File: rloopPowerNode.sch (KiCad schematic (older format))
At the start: 82 parts

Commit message: BMS added ctrl pins, both fault outputs to MCU, ...
added a few more comments for component selection

directions on net labels
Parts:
- removed JP? (x6): Jumper_NC_Small, symbol Jumper_NC_Small
- removed P?: CONN_01X02, symbol CONN_01X02
- removed Q?: NMOS, symbol Q_NMOS_GDSD
- added D? (x2): ZENER +3V6, symbol ZENER
- added D?: LED, symbol Led_Small
- added D?: D, symbol D_Small
- added R?: 1K8, symbol R
- added R?: 330, symbol R
- added R? (x2): 470, symbol R
- added R?: 100K, symbol R
- added R? (x2): 10K, symbol R
- D? (x2): Watts (none) -> 500mW
- Q?: Imax (none) -> 1A (4 * 250mA); Vgs Thresh (none) -> < 3V
- Q?: Vgs Thresh (none) -> > -3V
- R?: Power (none) -> 2W
- R?: Power (none) -> 8W
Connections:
- net labels added: BMS-CS, BMS-MISO, BMS-MOSI, BMS-PWRAVAIL, BMS-PWRDN, BMS-PWREN, BMS-SCK, GNDFAULT-PWM
- net labels removed: BMS-PWR, OSBMS-CS, OSBMS-MISO, OSBMS-MOSI, OSBMS-SCK
- wire segments 380 -> 394
- no-connect marks 3 -> 4
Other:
- note added: "Precharge\nminimizes arcing in relays"
- note removed: "connect to ISOMETER HV"
- note removed: "ground fault event\nwill kill all relays"
- moved on the sheet: C?, D?, P?, R?, U?

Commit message: added footprint
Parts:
- C1, C10, C2, C3, C4, C8, C9: renamed from C?; footprint (none) -> Capacitors_SMD:C_0603
- C5, C7: renamed from C?; footprint (none) -> SMD_Packages:SMD-1210_Pol
- C6: renamed from C?; footprint (none) -> Capacitors_SMD:C_0805
- D1, D10, D11, D3, D4, D7, D9: renamed from D?; footprint (none) -> Diodes_SMD:SOD-123
- D2, D8: renamed from D?; footprint (none) -> LEDs:LED_0603
- D5, D6: renamed from D?; footprint (none) -> Diodes_SMD:SMC_Standard
- JP1, JP2: renamed from JP?; footprint (none) -> -footprints:SOLDERJUMPER
- P22: renamed from P?; footprint (none) -> -footprints:AMPMODU-02X05-0.05in; symbol CONN_02X05 -> AMPMODU-02X05
- Q1: renamed from Q?; footprint (none) -> TO_SOT_Packages_SMD:SOT-23
- Q2: renamed from Q?; footprint (none) -> -footprints:D-Pak_TO252AA
- R1, R15, R17, R18, R19, R2, R20, R21, R3, R4, R5, R6, R7: renamed from R?; footprint (none) -> Resistors_SMD:R_0603
- R11, R12, R13, R14, R16: renamed from R?; footprint (none) -> Resistors_SMD:R_1206_HandSoldering
- U1, U2, U5, U6: renamed from U?; footprint (none) -> -footprints:CPC1718
- U10: renamed from U?; footprint (none) -> -footprints:SOIC-8-W
- U3: renamed from U?; footprint MFSOP-6 -> -footprints:OPTOCOUPLER-0.1in-6pin-SMD
- U4: renamed from U?; footprint (none) -> TO_SOT_Packages_SMD:SOT-23-5
- U7: renamed from U?; footprint (none) -> Housings_SOIC:SOIC-8_3.9x4.9mm_Pitch1.27mm
- U8: renamed from U?; footprint (none) -> -footprints:MS56xx
- U9: renamed from U?; footprint (none) -> TO_SOT_Packages_SMD:SOT89-3_Housing
- gave numbers to parts that had none: 31
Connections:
- wire segments 394 -> 329

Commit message: more parts assigned
just a check in for the meeting
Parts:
- F1: footprint (none) -> Fuse_Holders_and_Fuses:BladeFuse-CarType
- F2: footprint (none) -> Resistors_ThroughHole:Resistor_Horizontal_RM15mm
- JP3: footprint (none) -> Pin_Headers:Pin_Header_Straight_1x03
- P1, P19, P2, P20, P21, P23, P3, P4: footprint (none) -> -footprints:CONN-JST-XH-2-PTH-RGT
- P15, P16, P5: footprint (none) -> -footprints:SCREWPAD-4-40
- P17: footprint (none) -> -footprints:CONN-JST-XH-8-PTH-RGT
- P18, P6, P7: footprint (none) -> -footprints:CONN-TE-MICROMNL-2-PTH-MALE-RGT
- R10, R9: footprint (none) -> -footprints:D-Pak-TO252AA-Resistor
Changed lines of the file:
@@
 F 0 "P1" H 13400 1600 50  0000 C CNN
 F 1 "CONN_01X02" V 13500 1450 50  0000 C CNN
-F 2 "" H 13400 1450 50  0001 C CNN
+F 2 "-footprints:CONN-JST-XH-2-PTH-RGT" H 13400 1450 50  0001 C CNN
 F 3 "" H 13400 1450 50  0000 C CNN
 	1    13400 1450
@@
 F 0 "P3" H 13400 2750 50  0000 C CNN
 F 1 "CONN_01X02" V 13500 2600 50  0000 C CNN
-F 2 "" H 13400 2600 50  0001 C CNN
+F 2 "-footprints:CONN-JST-XH-2-PTH-RGT" H 13400 2600 50  0001 C CNN
 F 3 "" H 13400 2600 50  0000 C CNN
 	1    13400 2600
@@
 F 0 "P23" V 5650 9550 50  0000 C CNN
 F 1 "SHUNT" V 5550 9550 50  0000 C CNN
-F 2 "" H 5450 9550 50  0001 C CNN
+F 2 "-footprints:CONN-JST-XH-2-PTH-RGT" H 5450 9550 50  0001 C CNN
 F 3 "" H 5450 9550 50  0000 C CNN
 	1    5450 9550
@@
 F 0 "P21" H 5400 8300 50  0000 C CNN
 F 1 "CONN_01X02" V 5500 8150 50  0000 C CNN
-F 2 "" H 5400 8150 50  0001 C CNN
+F 2 "-footprints:CONN-JST-XH-2-PTH-RGT" H 5400 8150 50  0001 C CNN
 F 3 "" H 5400 8150 50  0000 C CNN
 	1    5400 8150
@@
 F 0 "P2" H 5100 1850 50  0000 C CNN
 F 1 "CONN_01X02" V 5200 1700 50  0001 C CNN
-F 2 "" H 5100 1700 50  0001 C CNN
+F 2 "-footprints:CONN-JST-XH-2-PTH-RGT" H 5100 1700 50  0001 C CNN
 F 3 "" H 5100 1700 50  0000 C CNN
 	1    5100 1700
@@
 F 0 "P4" H 13400 3900 50  0000 C CNN
 F 1 "CONN_01X02" V 13500 3750 50  0000 C CNN
-F 2 "" H 13400 3750 50  0001 C CNN
+F 2 "-footprints:CONN-JST-XH-2-PTH-RGT" H 13400 3750 50  0001 C CNN
 F 3 "" H 13400 3750 50  0000 C CNN
 	1    13400 3750
@@
 F 0 "P6" H 1350 5950 50  0000 C CNN
 F 1 "CONN_01X02" V 1450 5800 50  0001 C CNN
-F 2 "" H 1350 5800 50  0001 C CNN
+F 2 "-footprints:CONN-TE-MICROMNL-2-PTH-MALE-RGT" H 1350 5800 50  0001 C CNN
 F 3 "" H 1350 5800 50  0000 C CNN
 	1    1350 5800
@@
 F 0 "P7" H 2050 5950 50  0000 C CNN
 F 1 "CONN_01X02" V 2150 5800 50  0001 C CNN
-F 2 "" H 2050 5800 50  0001 C CNN
+F 2 "-footprints:CONN-TE-MICROMNL-2-PTH-MALE-RGT" H 2050 5800 50  0001 C CNN
 F 3 "" H 2050 5800 50  0000 C CNN
 	1    2050 5800
@@
 F 0 "P18" H 1350 8250 50  0000 C CNN
 F 1 "CONN_01X02" V 1450 8100 50  0001 C CNN
-F 2 "" H 1350 8100 50  0001 C CNN
+F 2 "-footprints:CONN-TE-MICROMNL-2-PTH-MALE-RGT" H 1350 8100 50  0001 C CNN
 F 3 "" H 1350 8100 50  0000 C CNN
 	1    1350 8100
@@
 F 0 "P17" H 13300 7750 50  0000 C CNN
 F 1 "CONN_01X08" V 13400 7300 50  0000 C CNN
-F 2 "" H 13300 7300 50  0001 C CNN
+F 2 "-footprints:CONN-JST-XH-8-PTH-RGT" H 13300 7300 50  0001 C CNN
 F 3 "" H 13300 7300 50  0000 C CNN
 	1    13300 7300
@@
 F 0 "P15" H 12550 7100 50  0000 C CNN
 F 1 "CONN_01X01" V 12500 7150 50  0001 C CNN
-F 2 "" H 12400 7150 50  0001 C CNN
+F 2 "-footprints:SCREWPAD-4-40" H 12400 7150 50  0001 C CNN
 F 3 "" H 12400 7150 50  0000 C CNN
 	1    12400 7150
@@
 F 0 "P16" H 12550 7200 50  0000 C CNN
 F 1 "CONN_01X01" V 12500 7250 50  0001 C CNN
-F 2 "" H 12400 7250 50  0001 C CNN
+F 2 "-footprints:SCREWPAD-4-40" H 12400 7250 50  0001 C CNN
 F 3 "" H 12400 7250 50  0000 C CNN
 	1    12400 7250
@@
 F 0 "JP3" H 8700 2850 50  0000 L CNN
 F 1 "JUMPER3" H 8650 3050 50  0000 C BNN
-F 2 "" H 8650 2950 50  0001 C CNN
+F 2 "Pin_Headers:Pin_Header_Straight_1x03" H 8650 2950 50  0001 C CNN
 F 3 "" H 8650 2950 50  0000 C CNN
 	1    8650 2950
@@
 F 0 "P5" H 2750 5450 50  0000 C CNN
 F 1 "CONN_01X01" V 2700 5400 50  0001 C CNN
-F 2 "" H 2600 5400 50  0001 C CNN
+F 2 "-footprints:SCREWPAD-4-40" H 2600 5400 50  0001 C CNN
 F 3 "" H 2600 5400 50  0000 C CNN
 	1    2600 5400
@@
 F 0 "R10" V 11530 5500 50  0000 C CNN
 F 1 "10" V 11450 5500 50  0000 C CNN
-F 2 "" V 11380 5500 50  0001 C CNN
+F 2 "-footprints:D-Pak-TO252AA-Resistor" V 11380 5500 50  0001 C CNN
 F 3 "" H 11450 5500 50  0000 C CNN
 F 4 "2W" V 11450 5500 60  0001 C CNN "Power"
@@
 F 0 "R9" V 9830 5500 50  0000 C CNN
 F 1 "100" V 9750 5500 50  0000 C CNN
-F 2 "" V 9680 5500 50  0001 C CNN
+F 2 "-footprints:D-Pak-TO252AA-Resistor" V 9680 5500 50  0001 C CNN
 F 3 "" H 9750 5500 50  0000 C CNN
 F 4 "8W" V 9750 5500 60  0001 C CNN "Power"
@@
 F 0 "F1" H 1600 6900 50  0000 C CNN
 F 1 "FUSE" H 1400 6800 50  0000 C CNN
-F 2 "" H 1500 6850 50  0001 C CNN
+F 2 "Fuse_Holders_and_Fuses:BladeFuse-CarType" H 1500 6850 50  0001 C CNN
 F 3 "" H 1500 6850 50  0000 C CNN
 	1    1500 6850
@@
 F 0 "F2" H 1600 7500 50  0000 C CNN
 F 1 "FUSE" H 1400 7400 50  0000 C CNN
-F 2 "" H 1500 7450 50  0001 C CNN
+F 2 "Resistors_ThroughHole:Resistor_Horizontal_RM15mm" H 1500 7450 50  0001 C CNN
 F 3 "" H 1500 7450 50  0000 C CNN
 	1    1500 7450
@@
 F 0 "P20" V 2650 8100 50  0000 C CNN
 F 1 "CONN_01X02" V 2650 8100 50  0001 C CNN
-F 2 "" H 2550 8100 50  0001 C CNN
+F 2 "-footprints:CONN-JST-XH-2-PTH-RGT" H 2550 8100 50  0001 C CNN
 F 3 "" H 2550 8100 50  0000 C CNN
 	1    2550 8100
@@
 F 0 "P19" V 2350 8100 50  0000 C CNN
 F 1 "CONN_01X02" V 2350 8100 50  0001 C CNN
-F 2 "" H 2250 8100 50  0001 C CNN
+F 2 "-footprints:CONN-JST-XH-2-PTH-RGT" H 2250 8100 50  0001 C CNN
 F 3 "" H 2250 8100 50  0000 C CNN
 	1    2250 8100
@@
 Precharge\nminimizes arcing in relays
 $Comp
-L GND #PWR?
+L GND #PWR049
 U 1 1 57346609
 P 3000 9550
-F 0 "#PWR?" H 3000 9300 50  0001 C CNN
+F 0 "#PWR049" H 3000 9300 50  0001 C CNN
 F 1 "GND" H 3000 9400 50  0000 C CNN
 F 2 "" H 3000 9550 50  0000 C CNN

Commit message: few connectors, cap dischg for DCDC, started layout
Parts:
- removed P12, P8, P9: CONN_01X01, symbol CONN_01X01
- removed P6: CONN_01X02, -footprints:CONN-TE-MICROMNL-2-PTH-MALE-RGT, symbol CONN_01X02
- added P6: CONN_01X04, -footprints:CONN-TE-MICROMNL-4-PTH-MALE-RGT, symbol CONN_01X04
- added P8, P9: CONN_01X02, -footprints:CONN-TE-MICROMNL-2-PTH-MALE-RGT, symbol CONN_01X02
- added R38: 1K, Resistors_SMD:R_1210, symbol R
- P22: footprint -footprints:AMPMODU-02X05-0.05in -> -footprints:AMPMODU-MALE-02X05-0.05in
- RL1: footprint (none) -> -footprints:RELAY-SOCKET-K10
- U9: footprint TO_SOT_Packages_SMD:SOT89-3_Housing -> -footprints:SOT89-3-VREG
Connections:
- net labels added: /GNDFAULT, RLY-IHV-HIGH, RLY-IHV-LOW
- net labels removed: RLY-ISO-HIGH, RLY-ISO-LOW, ~GNDFAULT
- wire segments 329 -> 335
- no-connect marks 4 -> 6
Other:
- moved on the sheet: C4, D10, D7, D8, D9, P15, P16, P17, P19, P20, P5, P7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

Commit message: wip some layout, added a diode to watchdog power
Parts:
- added D20: D_Schottky, Diodes_SMD:SOD-123, symbol D_Schottky
- F1: footprint Fuse_Holders_and_Fuses:BladeFuse-CarType -> Fuse_Holders_and_Fuses:Fuseholder5x20_horiz_open_universal_Type-III
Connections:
- wire segments 335 -> 336

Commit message: wip layout, most subcircuits
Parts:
- P6: symbol CONN_01X04 -> CONN_01X04-2XMNT
- P7, P8, P9: symbol CONN_01X02 -> CONN_01X02_2XMNT
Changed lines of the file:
@@
 Operate optoisolator LEDs at 30mA\nPerhaps a current limiter instead of resistor
 $Comp
-L CONN_01X02 P7
+L CONN_01X02_2XMNT P7
 U 1 1 5756A941
 P 2200 5800
@@
 F 4 "8W" V 9750 5500 60  0001 C CNN "Power"
 	1    9750 5500
-	0    1    1    0
+	0    -1   -1   0
 $EndComp
 $Comp
@@
 	1500 5600 1500 5500
 $Comp
-L CONN_01X04 P6
+L CONN_01X04-2XMNT P6
 U 1 1 57312237
 P 1450 5800
@@
 $EndComp
 $Comp
-L CONN_01X02 P8
+L CONN_01X02_2XMNT P8
 U 1 1 57318BE2
 P 10200 6250
@@
 BATT-NEG
 $Comp
-L CONN_01X02 P9
+L CONN_01X02_2XMNT P9
 U 1 1 5731F074
 P 11900 6250
@@
 Wire Wire Line
 	6800 2400 9650 2400
+Text Label 1650 5800 0    4    ~ 0
+BATT-NEG
+Text Label 1250 5800 0    4    ~ 0
+BATT-NEG
+Text Label 10200 6150 0    4    ~ 0
+BATT-NEG
+Text Label 10200 6350 0    4    ~ 0
+BATT-NEG
+Text Label 11900 6150 0    4    ~ 0
+BATT-NEG
+Text Label 11900 6350 0    4    ~ 0
+BATT-NEG
+Text Label 2100 5800 0    4    ~ 0
+GND
+Text Label 2300 5800 0    4    ~ 0
+GND
 $EndSCHEMATC

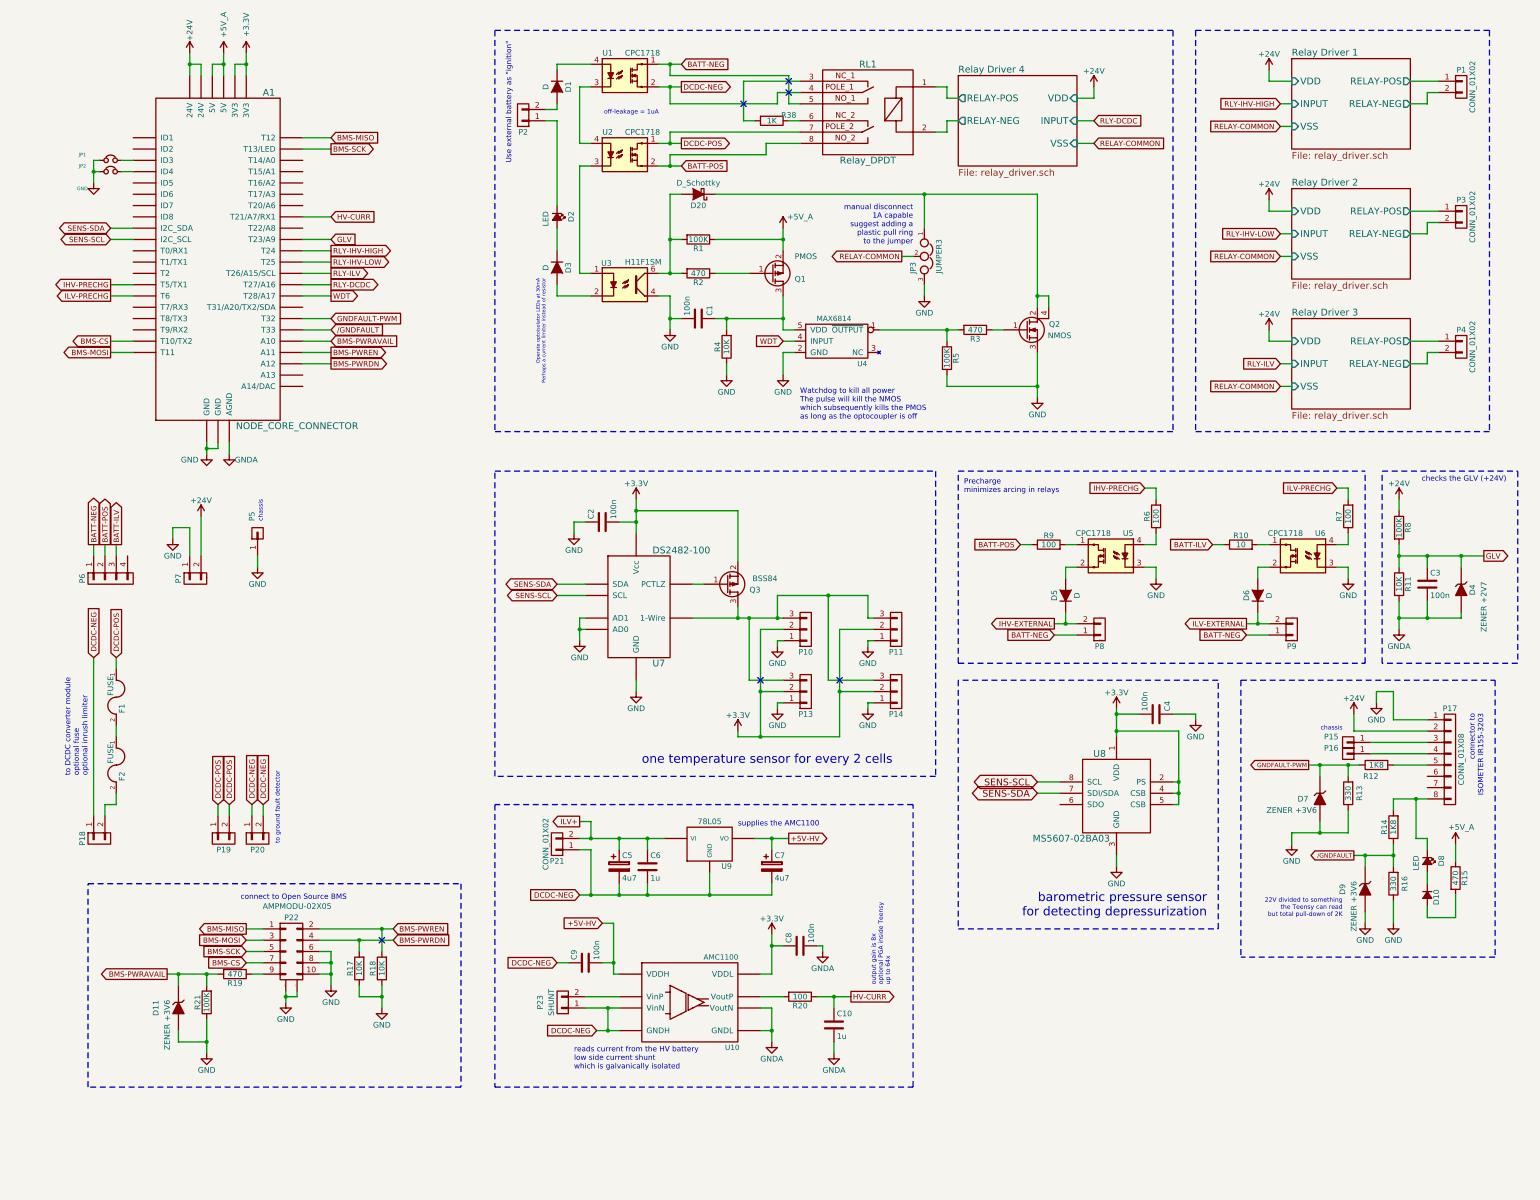
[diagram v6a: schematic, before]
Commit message: wip, bigger pads on relays, placed sensors
HV current sensor flipped polarity
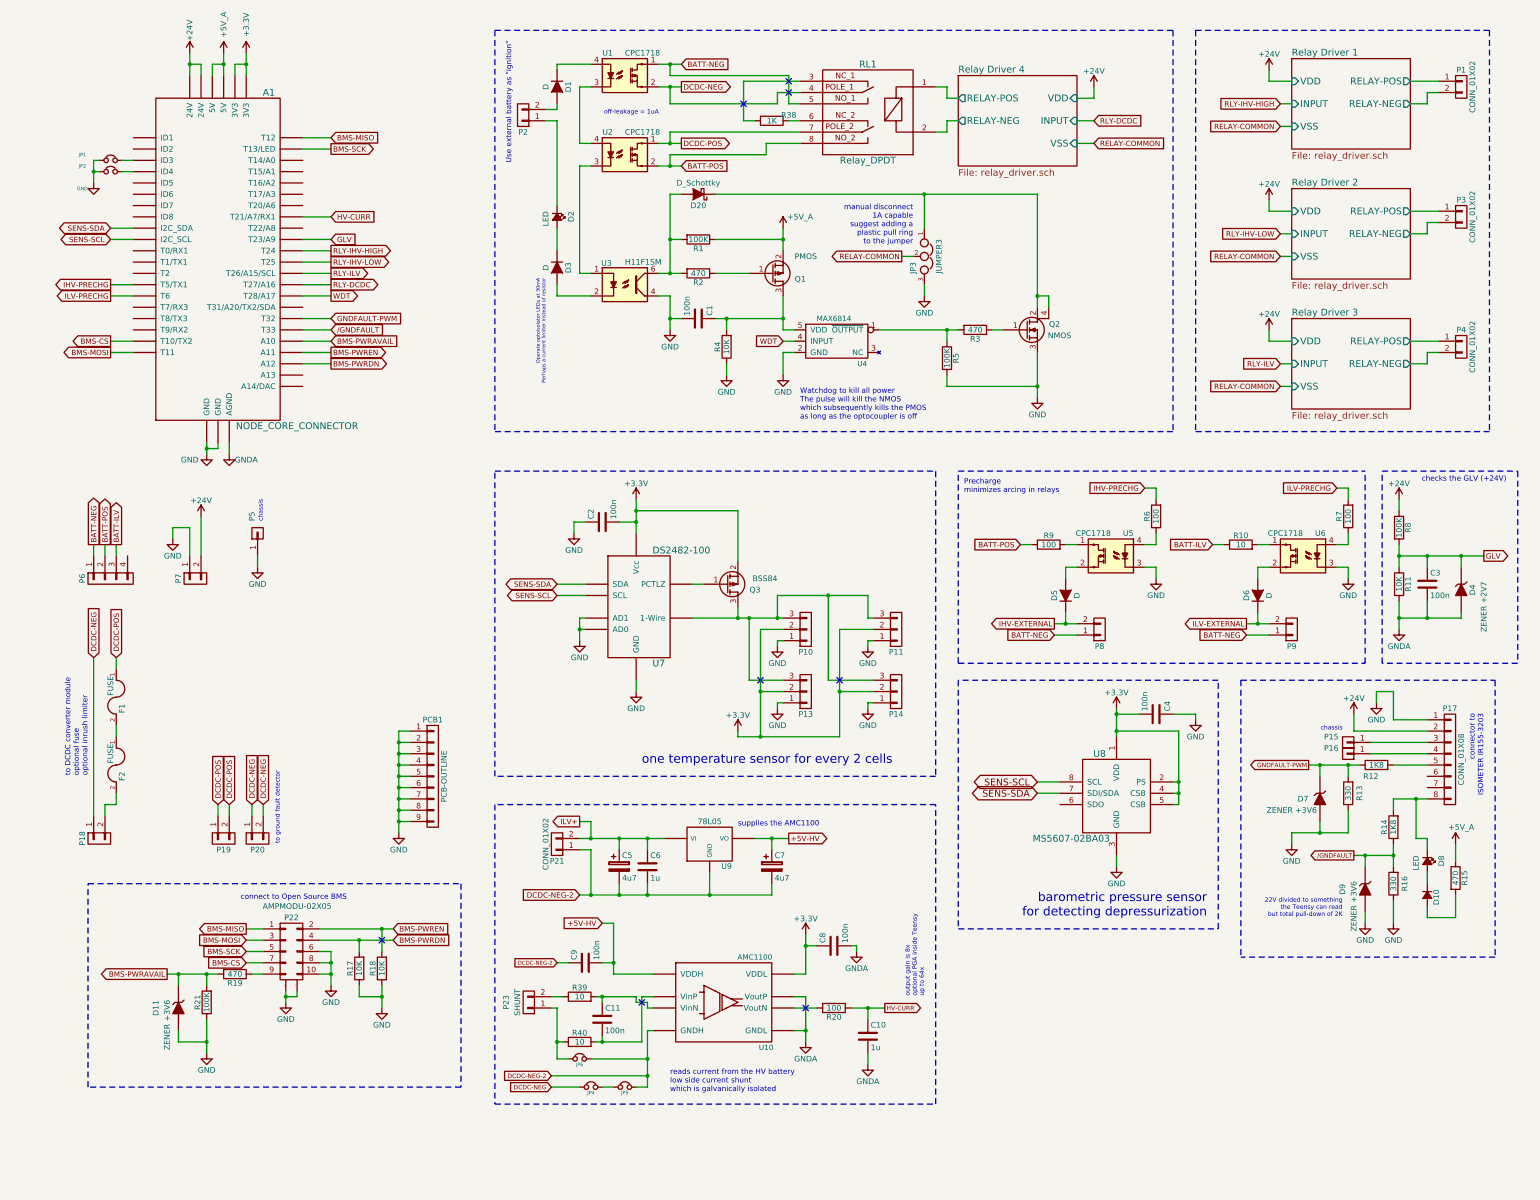
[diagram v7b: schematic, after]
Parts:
- added C11: 100n, Capacitors_SMD:C_0603, symbol C
- added JP4, JP5, JP6: Jumper_NC_Small, -footprints:SOLDERJUMPER, symbol Jumper_NC_Small
- added PCB1: PCB-OUTLINE, -footprints:PCBOUTLINE-POWERNODE, symbol CONN_01X09
- added R39, R40: 10, Resistors_SMD:R_0603, symbol R
- C8, C9: footprint Capacitors_SMD:C_0603 -> Capacitors_SMD:C_1206
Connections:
- net DCDC-NEG: now also JP4.1; no longer C5.2, C6.2, C7.2, C9.1, P21.1 (P1), P23.1 (P1), U10.3 (VinN), U10.4 (GNDH), U9.GND
- net GND: now also PCB1.1 (P1), PCB1.2 (P2), PCB1.3 (P3), PCB1.4 (P4), PCB1.5 (P5), PCB1.6 (P6), PCB1.7 (P7), PCB1.8 (P8), PCB1.9 (P9)
- net GNDA: now also U10.7 (VoutP); no longer U10.6 (VoutN)
- net at P23.2 (P2): now also R39.1; no longer U10.2 (VinP)
- net at R20.2: now also U10.6 (VoutN); no longer U10.7 (VoutP)
- new net: C11.1, R39.2, U10.3 (VinN)
- new net: JP6.1, P23.1 (P1), R40.1
- new net: C11.2, R40.2, U10.2 (VinP)
- new net: JP4.2, JP5.1
- new net DCDC-NEG-2: C5.2, C6.2, C7.2, C9.1, JP5.2, JP6.2, P21.1 (P1), U10.4 (GNDH), U9.GND
- no-connect marks 6 -> 8
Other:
- moved on the sheet: C10, C8, P23, R20, U10
